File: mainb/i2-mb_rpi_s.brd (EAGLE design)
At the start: 110 x 106.6 mm, 37 parts, among them IC3 DS1307Z, T1 BC337, T2 BC337, X9 eth (mb->rpi)

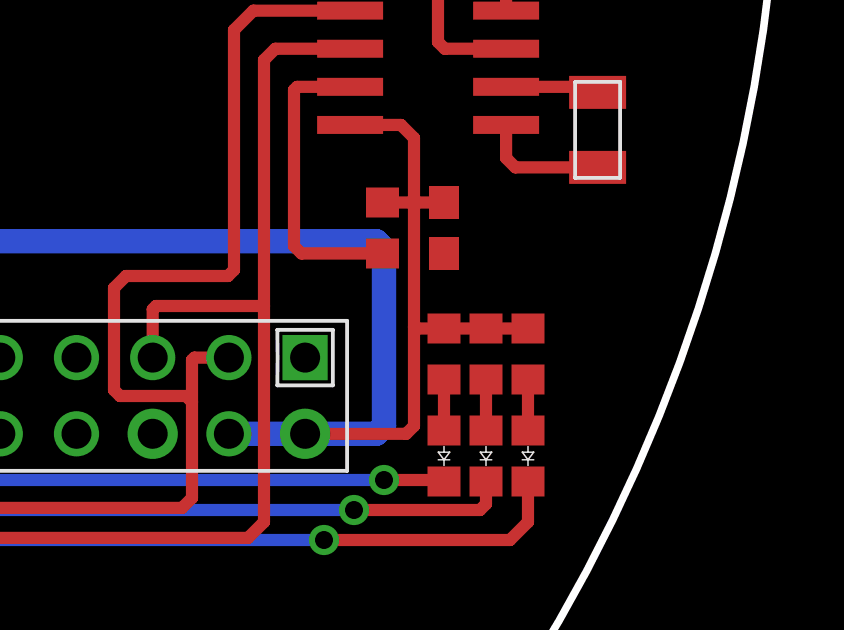
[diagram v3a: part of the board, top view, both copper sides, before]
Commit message: mainb: 8) leds -> 3V3
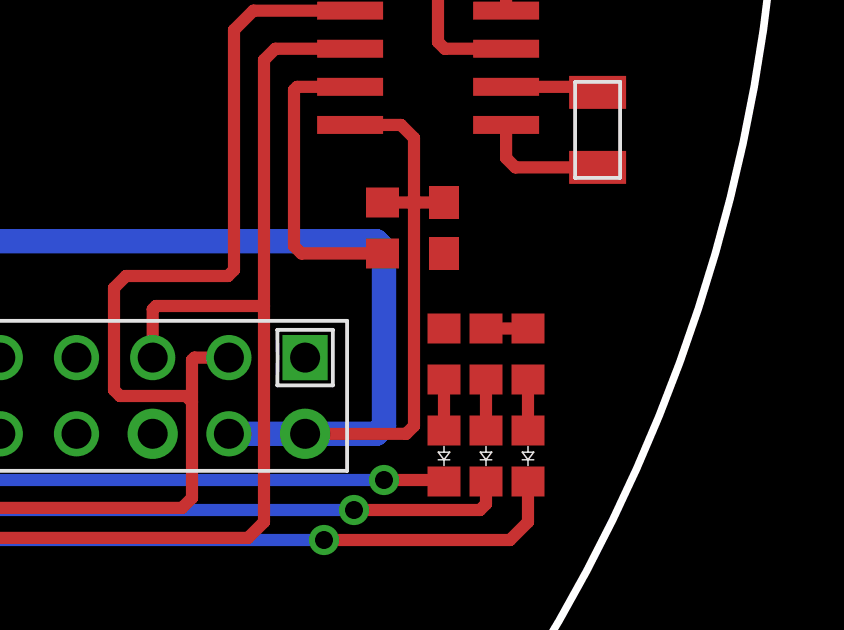
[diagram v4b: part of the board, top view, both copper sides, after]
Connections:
- new net N$11: R4.2, R5.2, R6.2, U$2.1
- net +5V_RPI: no longer R4.2, R5.2, R6.2
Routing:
- net +5V_RPI: track 114.0 -> 110.1 mm
- net N$11: track 0.00 -> 1.45 mm
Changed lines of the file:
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@@
 <wire x1="42.365" y1="-10.965" x2="42.8" y2="-11.4" width="0.4064" layer="1"/>
 <wire x1="42.8" y1="-11.4" x2="42.8" y2="-13.6" width="0.4064" layer="1"/>
-<wire x1="42.8" y1="-13.6" x2="42.8" y2="-17.7" width="0.4064" layer="1"/>
-<wire x1="42.8" y1="-17.7" x2="42.8" y2="-21" width="0.4064" layer="1"/>
+<wire x1="42.8" y1="-13.6" x2="42.8" y2="-21" width="0.4064" layer="1"/>
 <wire x1="39.17" y1="-21.26" x2="42.54" y2="-21.26" width="0.4064" layer="1"/>
 <wire x1="39.17" y1="-21.26" x2="41.54" y2="-21.26" width="0.8128" layer="16"/>
@@
 <wire x1="36.63" y1="-21.26" x2="39.17" y2="-21.26" width="0.8128" layer="16"/>
 <contactref element="C1" pad="1"/>
-<contactref element="R5" pad="2"/>
-<contactref element="R6" pad="2"/>
 <contactref element="R7" pad="1"/>
-<contactref element="R4" pad="2"/>
 <wire x1="41.75" y1="-13.55" x2="42.75" y2="-13.55" width="0.4064" layer="1"/>
 <wire x1="39.2" y1="-21.29" x2="39.17" y2="-21.26" width="0.4064" layer="1"/>
@@
 <wire x1="43.8" y1="-13.55" x2="42.85" y2="-13.55" width="0.4064" layer="1"/>
 <wire x1="42.85" y1="-13.55" x2="42.8" y2="-13.6" width="0.4064" layer="1"/>
-<wire x1="46.6" y1="-17.75" x2="45.2" y2="-17.75" width="0.4064" layer="1"/>
-<wire x1="45.2" y1="-17.75" x2="45.15" y2="-17.75" width="0.4064" layer="1"/>
-<wire x1="45.2" y1="-17.75" x2="43.8" y2="-17.75" width="0.4064" layer="1"/>
-<wire x1="43.8" y1="-17.75" x2="42.85" y2="-17.75" width="0.4064" layer="1"/>
-<wire x1="42.85" y1="-17.75" x2="42.8" y2="-17.7" width="0.4064" layer="1"/>
 <wire x1="0" y1="-11.2" x2="-5.6" y2="-12.47" width="0" layer="19" extent="16-16"/>
 </signal>
@@
 <wire x1="46.6" y1="-24.2" x2="46" y2="-24.8" width="0.4064" layer="1"/>
 </signal>
+<signal name="N$11">
+<contactref element="R6" pad="2"/>
+<contactref element="R4" pad="2"/>
+<wire x1="46.6" y1="-17.75" x2="45.2" y2="-17.75" width="0.4064" layer="1"/>
+<wire x1="45.2" y1="-17.75" x2="45.15" y2="-17.75" width="0.4064" layer="1"/>
+<contactref element="R5" pad="2"/>
+<contactref element="U$2" pad="1"/>
+<wire x1="43.8" y1="-17.75" x2="45.15" y2="-17.75" width="0" layer="19" extent="1-1"/>
+<wire x1="39.17" y1="-18.72" x2="43.8" y2="-17.75" width="0" layer="19" extent="1-1"/>
+</signal>
 </signals>

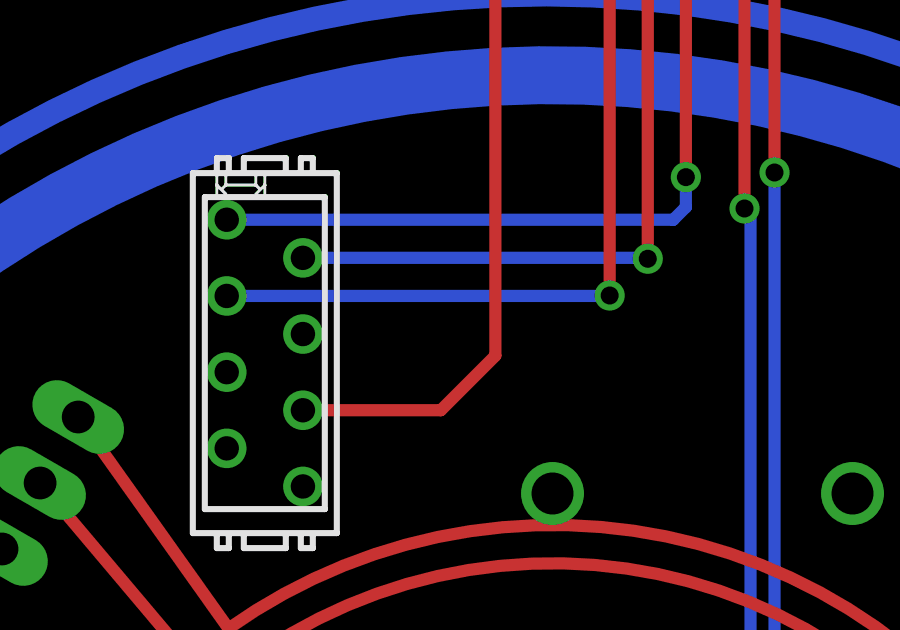
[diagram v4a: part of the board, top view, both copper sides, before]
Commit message: mainb: 7) eth. conn. order
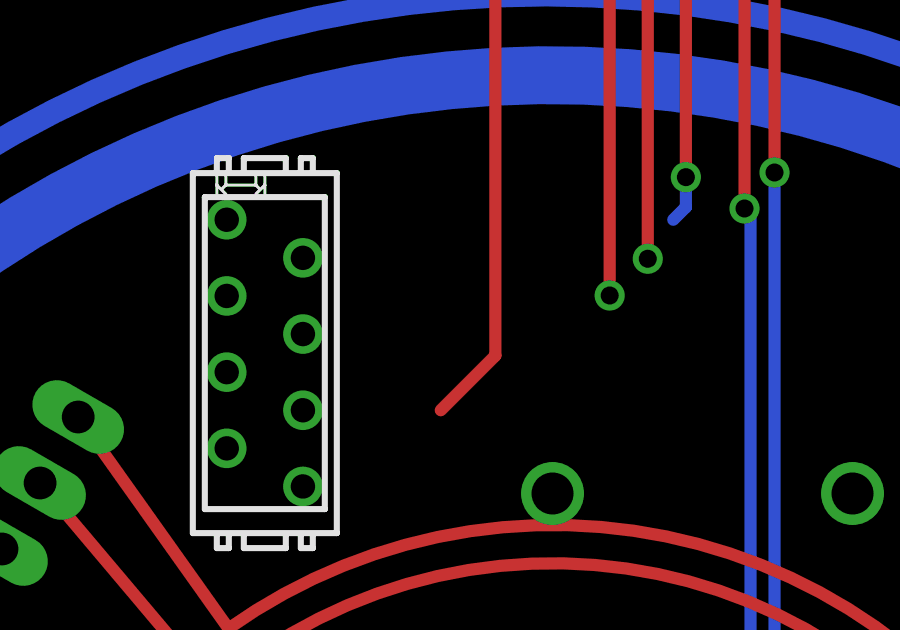
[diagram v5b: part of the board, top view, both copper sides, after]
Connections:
- net RX+: now also X9.4; no longer X9.3
- net TX-: now also X9.3; no longer X9.2
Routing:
- net TX+: track 27.0 -> 12.1 mm
- net RX+: track 27.3 -> 14.5 mm
- net TX-: track 22.2 -> 10.8 mm
- net RX-: track 21.1 -> 16.5 mm
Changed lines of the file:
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@@
 <signal name="TX+">
 <contactref element="X_ETH" pad="1"/>
-<contactref element="X9" pad="1"/>
 <wire x1="4.445" y1="40.79" x2="4.445" y2="30.245" width="0.4064" layer="1"/>
-<wire x1="-10.86" y1="28.825" x2="4.025" y2="28.825" width="0.4064" layer="16"/>
 <via x="4.445" y="30.245" extent="1-16" drill="0.6"/>
 <wire x1="4.445" y1="30.245" x2="4.445" y2="29.245" width="0.4064" layer="16"/>
 <wire x1="4.445" y1="29.245" x2="4.025" y2="28.825" width="0.4064" layer="16"/>
+<contactref element="X9" pad="1"/>
+<wire x1="-10.86" y1="28.825" x2="4.025" y2="28.825" width="0" layer="19" extent="16-16"/>
 </signal>
 <signal name="TX-">
 <contactref element="X_ETH" pad="2"/>
-<contactref element="X9" pad="2"/>
 <wire x1="3.175" y1="38.25" x2="3.175" y2="27.525" width="0.4064" layer="1"/>
 <via x="3.175" y="27.525" extent="1-16" drill="0.6"/>
-<wire x1="-8.32" y1="27.555" x2="3.145" y2="27.555" width="0.4064" layer="16"/>
 <wire x1="3.145" y1="27.555" x2="3.175" y2="27.525" width="0.4064" layer="16"/>
+<contactref element="X9" pad="3"/>
+<wire x1="-10.86" y1="26.285" x2="3.145" y2="27.555" width="0" layer="19" extent="16-16"/>
 </signal>
 <signal name="RX+">
 <contactref element="X_ETH" pad="3"/>
-<contactref element="X9" pad="3"/>
 <wire x1="1.905" y1="40.79" x2="1.905" y2="26.3" width="0.4064" layer="1"/>
-<wire x1="-10.86" y1="26.285" x2="1.905" y2="26.285" width="0.4064" layer="16"/>
 <via x="1.905" y="26.3" extent="1-16" drill="0.6"/>
 <wire x1="1.905" y1="26.3" x2="1.905" y2="26.285" width="0.4064" layer="16"/>
+<contactref element="X9" pad="4"/>
+<wire x1="-8.32" y1="25.015" x2="1.905" y2="26.3" width="0" layer="19" extent="1-1"/>
 </signal>
 <signal name="RX-">
 <contactref element="X_ETH" pad="6"/>
-<contactref element="X9" pad="6"/>
 <wire x1="-1.905" y1="38.25" x2="-1.905" y2="24.295" width="0.4064" layer="1"/>
 <wire x1="-1.905" y1="24.295" x2="-3.725" y2="22.475" width="0.4064" layer="1"/>
-<wire x1="-8.32" y1="22.475" x2="-3.725" y2="22.475" width="0.4064" layer="1"/>
+<contactref element="X9" pad="6"/>
+<wire x1="-8.32" y1="22.475" x2="-3.725" y2="22.475" width="0" layer="19" extent="1-1"/>
 </signal>
 <signal name="+12V_IN">

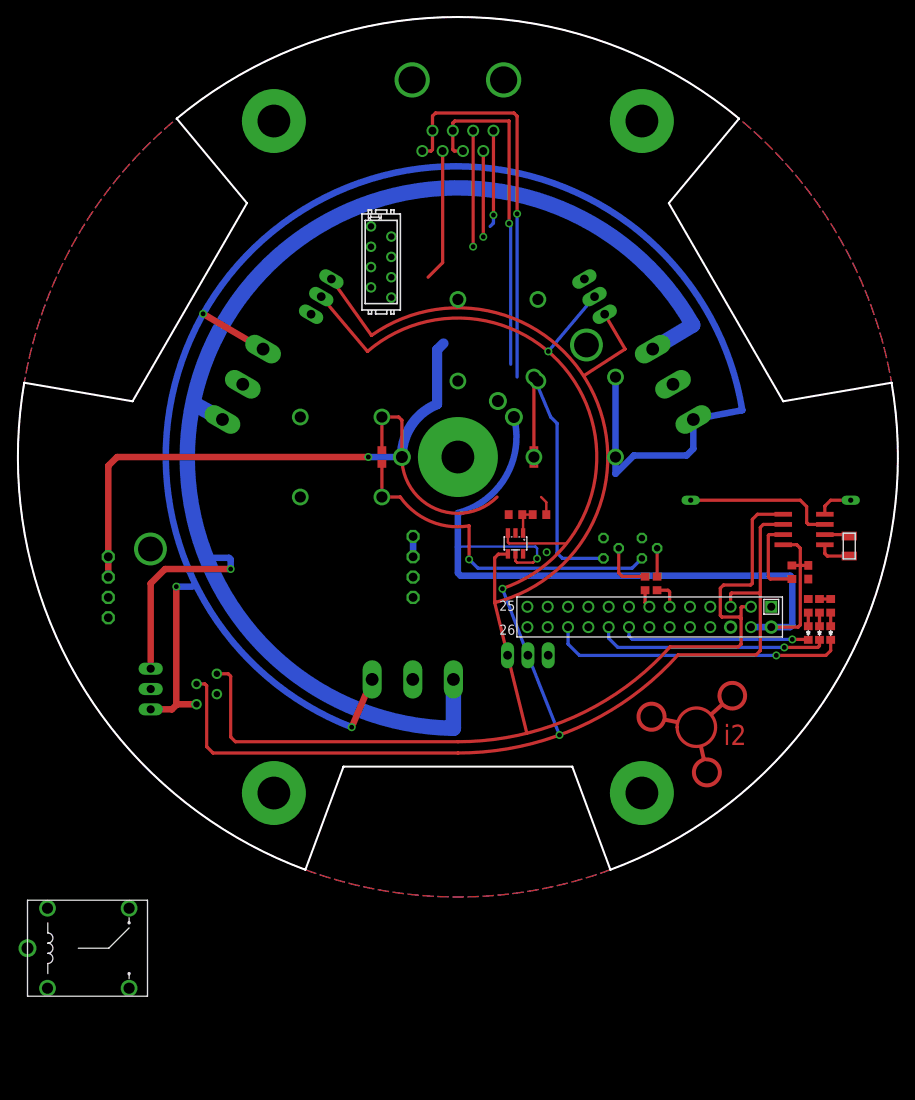
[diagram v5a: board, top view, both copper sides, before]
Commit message: mainb: 9) battery holder wholes dia
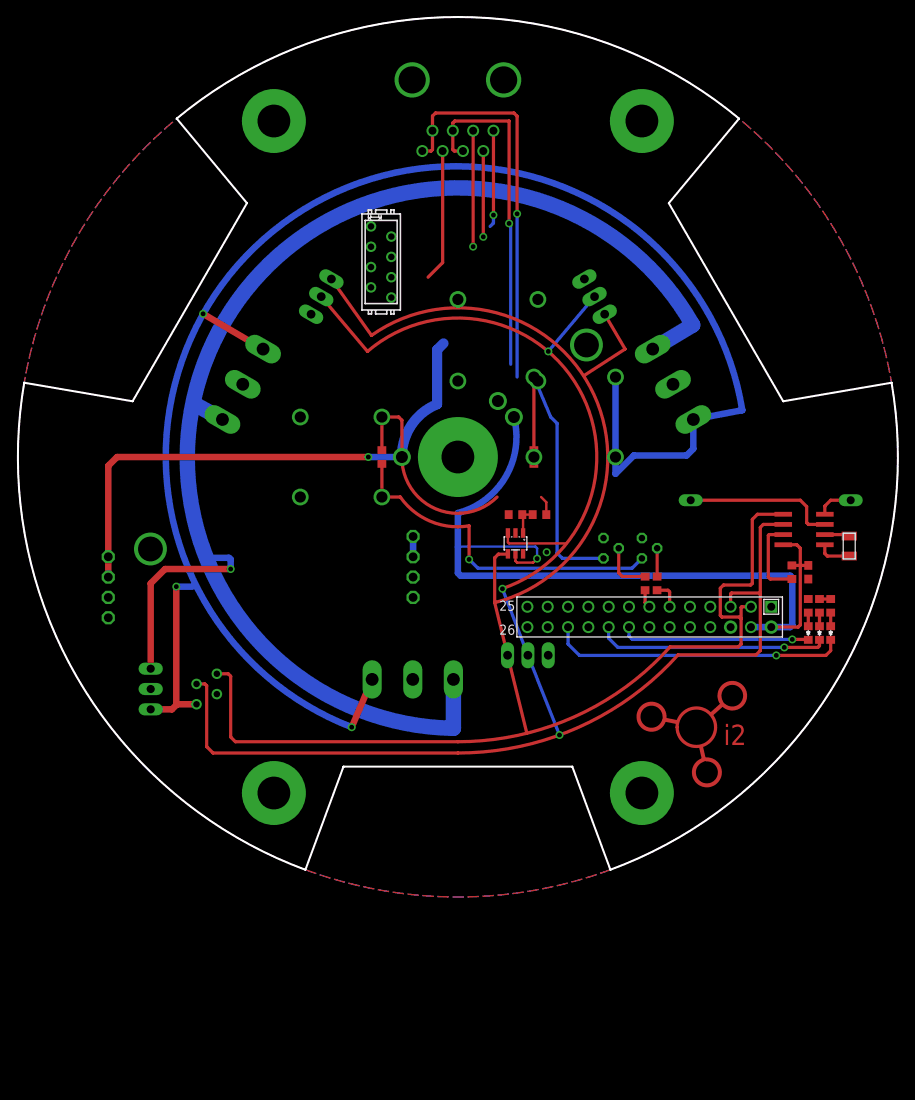
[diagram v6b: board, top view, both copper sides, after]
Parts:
- removed U$9: FBR51, wb:PC_RELAY
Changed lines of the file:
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@@
 </element>
 <element name="U$1" library="isfar2-logo" package="I2-LOGO" value="" x="30" y="-33.4"/>
-<element name="U$9" library="wb" package="PC_RELAY" value="FBR51" x="-53.8" y="-61.4"/>
 </elements>
 <signals>

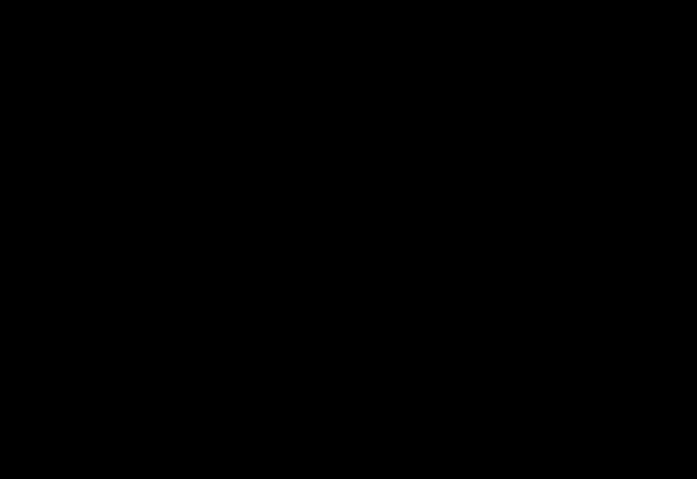
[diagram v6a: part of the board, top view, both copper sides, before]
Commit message: mainb: 10) RPi UART for debugging
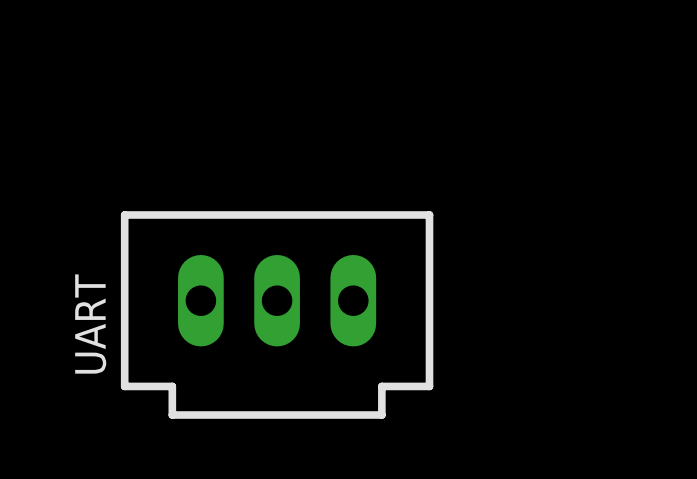
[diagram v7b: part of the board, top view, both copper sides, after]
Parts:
- added UART: C-GRID-03-70543, con-molex:70543-03
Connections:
- new net RX: U$2.10, UART.2
- new net TX: U$2.8, UART.3
- net GND: now also UART.1
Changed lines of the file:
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@@
 </element>
 <element name="U$1" library="isfar2-logo" package="I2-LOGO" value="" x="30" y="-33.4"/>
+<element name="UART" library="con-molex" package="70543-03" value="C-GRID-03-70543" x="-48" y="-59.8">
+<attribute name="OC_NEWARK" value="unknown" x="-48" y="-59.8" size="1.778" layer="27" display="off"/>
+<attribute name="MPN" value="" x="-48" y="-59.8" size="1.778" layer="27" display="off"/>
+<attribute name="MF" value="" x="-48" y="-59.8" size="1.778" layer="27" display="off"/>
+<attribute name="OC_FARNELL" value="unknown" x="-48" y="-59.8" size="1.778" layer="27" display="off"/>
+</element>
 </elements>
 <signals>
@@
 <contactref element="I2C_3" pad="3"/>
 <contactref element="I2C_1" pad="3"/>
+<contactref element="UART" pad="1"/>
+<wire x1="-23" y1="-42" x2="-50.54" y2="-59.8" width="0" layer="19" extent="1-1"/>
+<wire x1="-30.13" y1="-29.635" x2="-23" y2="-42" width="0" layer="19" extent="1-1"/>
+<wire x1="-38.4" y1="-29" x2="-30.13" y2="-29.635" width="0" layer="19" extent="1-1"/>
+<wire x1="-43.7" y1="-20.09" x2="-38.4" y2="-29" width="0" layer="19" extent="1-1"/>
+<wire x1="-43.7" y1="-17.55" x2="-43.7" y2="-20.09" width="0" layer="19" extent="1-1"/>
+<wire x1="-5.64" y1="-27.8" x2="-23" y2="-42" width="0" layer="19" extent="1-1"/>
+<wire x1="-5.6" y1="-17.55" x2="-5.64" y2="-27.8" width="0" layer="19" extent="1-1"/>
+<wire x1="-5.6" y1="-15.01" x2="-5.6" y2="-17.55" width="0" layer="19" extent="1-1"/>
+<wire x1="7.2" y1="-9.4999" x2="-5.6" y2="-15.01" width="0" layer="19" extent="1-1"/>
+<wire x1="6.35" y1="-7.2" x2="7.2" y2="-9.4999" width="0" layer="19" extent="1-1"/>
+<wire x1="8.15" y1="-12.1001" x2="7.2" y2="-9.4999" width="0" layer="19" extent="1-1"/>
+<wire x1="11.1" y1="-11.9" x2="8.15" y2="-12.1001" width="0" layer="19" extent="1-1"/>
+<wire x1="8.69" y1="-18.72" x2="8.15" y2="-12.1001" width="0" layer="19" extent="1-1"/>
+<wire x1="11.29" y1="-24.78" x2="8.69" y2="-18.72" width="0" layer="19" extent="1-1"/>
+<wire x1="16.31" y1="-21.26" x2="11.29" y2="-24.78" width="0" layer="19" extent="1-1"/>
+<wire x1="18.2" y1="-10.13" x2="11.1" y2="-11.9" width="0" layer="19" extent="1-1"/>
+<wire x1="23" y1="-10.13" x2="18.2" y2="-10.13" width="0" layer="19" extent="1-1"/>
+<wire x1="23.93" y1="-21.26" x2="16.31" y2="-21.26" width="0" layer="19" extent="1-1"/>
+<wire x1="29.01" y1="-18.72" x2="23.93" y2="-21.26" width="0" layer="19" extent="1-1"/>
+<wire x1="34.09" y1="-21.26" x2="29.01" y2="-18.72" width="0" layer="19" extent="1-1"/>
+<wire x1="43.8" y1="-15.25" x2="34.09" y2="-21.26" width="0" layer="19" extent="1-1"/>
+<wire x1="45.87" y1="-7.155" x2="43.8" y2="-15.25" width="0" layer="19" extent="1-1"/>
+<wire x1="0" y1="9.5" x2="6.35" y2="-7.2" width="0" layer="19" extent="1-1"/>
+<wire x1="26.89" y1="9.09" x2="23" y2="-10.13" width="0" layer="19" extent="1-1"/>
+<wire x1="15.8108875" y1="22.249703125" x2="26.89" y2="9.09" width="0" layer="19" extent="1-1"/>
+<wire x1="-18.3508875" y1="17.85029375" x2="0" y2="9.5" width="0" layer="19" extent="1-1"/>
+<wire x1="-26.89" y1="9.09" x2="-18.3508875" y2="17.85029375" width="0" layer="19" extent="1-1"/>
+<wire x1="23" y1="-42" x2="23.93" y2="-21.26" width="0" layer="19" extent="1-1"/>
+<wire x1="23" y1="42" x2="15.8108875" y2="22.249703125" width="0" layer="19" extent="1-1"/>
+<wire x1="-23" y1="42" x2="-18.3508875" y2="17.85029375" width="0" layer="19" extent="1-1"/>
 </signal>
 <signal name="N$1">
@@
 <wire x1="39.17" y1="-18.72" x2="43.8" y2="-17.75" width="0" layer="19" extent="1-1"/>
 </signal>
+<signal name="TX">
+<contactref element="UART" pad="3"/>
+<contactref element="U$2" pad="8"/>
+<wire x1="31.55" y1="-21.26" x2="-45.46" y2="-59.8" width="0" layer="19" extent="1-1"/>
+</signal>
+<signal name="RX">
+<contactref element="UART" pad="2"/>
+<contactref element="U$2" pad="10"/>
+<wire x1="29.01" y1="-21.26" x2="-48" y2="-59.8" width="0" layer="19" extent="1-1"/>
+</signal>
 </signals>

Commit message: trinocular/rpicam/ added
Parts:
- added LED4, LED5: (no value), wb:D0603
- added R8, R9: 500, rcl:R0603
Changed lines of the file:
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@@
 <attribute name="OC_FARNELL" value="unknown" x="-48" y="-59.8" size="1.778" layer="27" display="off"/>
 </element>
+<element name="LED4" library="wb" package="D0603" value="" x="-53.6" y="-66.2"/>
+<element name="R8" library="rcl" package="R0603" value="500" x="-53.6" y="-69.6"/>
+<element name="LED5" library="wb" package="D0603" value="" x="-53.6" y="-74.4"/>
+<element name="R9" library="rcl" package="R0603" value="500" x="-53.6" y="-77.8"/>
 </elements>
 <signals>
